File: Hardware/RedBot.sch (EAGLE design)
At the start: 40 parts, among them U1 ATMEGA328P, U2 TB6612FNG, U3 MIC5219 5V

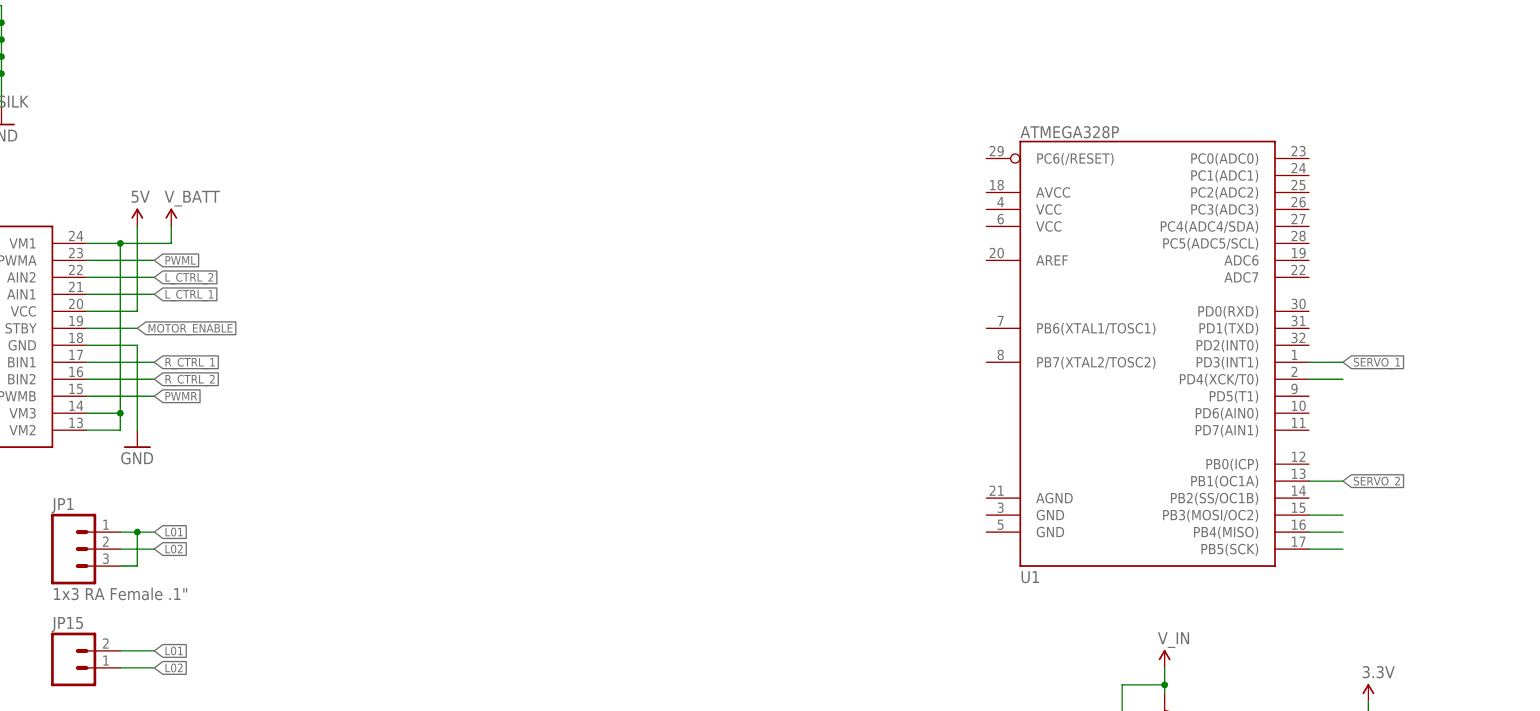
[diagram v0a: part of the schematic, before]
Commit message: Updated motor ic to use 3.3V
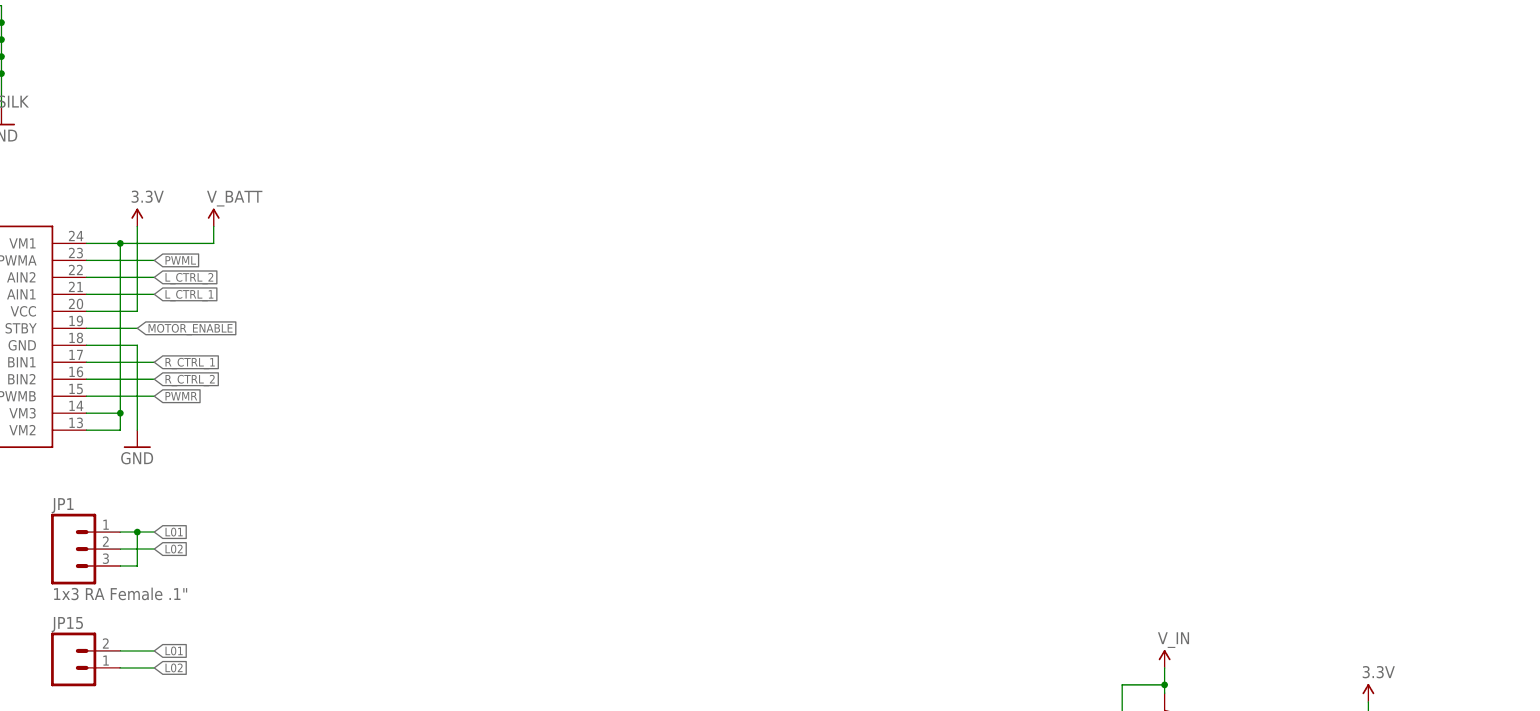
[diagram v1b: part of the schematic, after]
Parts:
- removed U1: ATMEGA328P, SparkFun-DigitalIC:ATMEGA328_SMT
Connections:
- removed net MISO: U1.PB4(MISO)
- removed net SCK: U1.PB5(SCK)
- removed net SERVO_4/MOSI: U1.PB3(MOSI/OC2)
- net 3.3V: now also U2.VCC
- net 5V: no longer U2.VCC
- net L_CTRL_2: no longer U1.PD4(XCK/T0)
- net SERVO_1: no longer U1.PD3(INT1)
- net SERVO_2: no longer U1.PB1(OC1A)
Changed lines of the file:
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@@
 <parts>
 <part name="FRAME1" library="SparkFun-Aesthetics" deviceset="FRAME-LETTER" device=""/>
-<part name="U1" library="SparkFun-DigitalIC" deviceset="ATMEGA328_SMT" device="" value="ATMEGA328P"/>
 <part name="C2" library="SparkFun-Capacitors" deviceset="0.1UF-25V(+80/-20%)(0603)" device="" value="0.1uF"/>
 <part name="C3" library="SparkFun-Capacitors" deviceset="0.1UF-25V(+80/-20%)(0603)" device="" value="0.1uF"/>
@@
 <part name="U$5" library="SparkFun-Aesthetics" deviceset="5V" device="" value="V_IN"/>
 <part name="U$7" library="SparkFun-Aesthetics" deviceset="V_BATT" device=""/>
-<part name="U$8" library="SparkFun-Aesthetics" deviceset="5V" device=""/>
+<part name="3.3V" library="SparkFun-Aesthetics" deviceset="5V" device="" value="3.3V"/>
 <part name="GND6" library="SparkFun-Aesthetics" deviceset="GND" device=""/>
 <part name="GND7" library="SparkFun-Aesthetics" deviceset="GND" device=""/>
@@
 <instances>
 <instance part="FRAME1" gate="G$2" x="304.8" y="0"/>
-<instance part="U1" gate="G$1" x="236.22" y="129.54"/>
 <instance part="C2" gate="G$1" x="300.99" y="63.5"/>
 <instance part="C3" gate="G$1" x="311.15" y="63.5"/>
@@
 <instance part="GND4" gate="1" x="240.03" y="10.16"/>
 <instance part="U$5" gate="G$1" x="240.03" y="78.74"/>
-<instance part="U$7" gate="G$1" x="91.44" y="144.78"/>
-<instance part="U$8" gate="G$1" x="86.36" y="144.78"/>
+<instance part="U$7" gate="G$1" x="97.79" y="144.78"/>
+<instance part="3.3V" gate="G$1" x="86.36" y="144.78"/>
 <instance part="GND6" gate="1" x="86.36" y="111.76"/>
 <instance part="GND7" gate="1" x="40.64" y="111.76"/>
@@
 <net name="SERVO_1" class="0">
 <segment>
-<pinref part="U1" gate="G$1" pin="PD3(INT1)"/>
-<wire x1="261.62" y1="124.46" x2="266.7" y2="124.46" width="0.1524" layer="91"/>
-<label x="266.7" y="124.46" size="1.27" layer="95" xref="yes"/>
-</segment>
-<segment>
 <pinref part="JP8" gate="G$1" pin="1"/>
 <wire x1="353.06" y1="185.42" x2="342.9" y2="185.42" width="0.1524" layer="91"/>
@@
 <net name="SERVO_2" class="0">
 <segment>
-<pinref part="U1" gate="G$1" pin="PB1(OC1A)"/>
-<wire x1="261.62" y1="106.68" x2="266.7" y2="106.68" width="0.1524" layer="91"/>
-<label x="266.7" y="106.68" size="1.27" layer="95" xref="yes"/>
-</segment>
-<segment>
 <pinref part="JP8" gate="G$1" pin="2"/>
 <wire x1="368.3" y1="185.42" x2="378.46" y2="185.42" width="0.1524" layer="91"/>
@@
 <wire x1="391.16" y1="231.14" x2="393.7" y2="231.14" width="0.1524" layer="91"/>
 <label x="393.7" y="231.14" size="1.27" layer="95" xref="yes"/>
-</segment>
-</net>
-<net name="SERVO_4/MOSI" class="0">
-<segment>
-<pinref part="U1" gate="G$1" pin="PB3(MOSI/OC2)"/>
-<wire x1="261.62" y1="101.6" x2="266.7" y2="101.6" width="0.1524" layer="91"/>
-</segment>
-</net>
-<net name="MISO" class="0">
-<segment>
-<pinref part="U1" gate="G$1" pin="PB4(MISO)"/>
-<wire x1="261.62" y1="99.06" x2="266.7" y2="99.06" width="0.1524" layer="91"/>
-</segment>
-</net>
-<net name="SCK" class="0">
-<segment>
-<pinref part="U1" gate="G$1" pin="PB5(SCK)"/>
-<wire x1="261.62" y1="96.52" x2="266.7" y2="96.52" width="0.1524" layer="91"/>
 </segment>
 </net>
@@
 </segment>
 <segment>
-<pinref part="U2" gate="G$1" pin="VCC"/>
-<wire x1="78.74" y1="132.08" x2="86.36" y2="132.08" width="0.1524" layer="91"/>
-<pinref part="U$8" gate="G$1" pin="5V"/>
-<wire x1="86.36" y1="132.08" x2="86.36" y2="144.78" width="0.1524" layer="91"/>
-</segment>
-<segment>
 <pinref part="R8" gate="G$1" pin="2"/>
 <wire x1="20.32" y1="231.14" x2="15.24" y2="231.14" width="0.1524" layer="91"/>
@@
 </segment>
 <segment>
-<pinref part="U1" gate="G$1" pin="PD4(XCK/T0)"/>
-<wire x1="261.62" y1="121.92" x2="266.7" y2="121.92" width="0.1524" layer="91"/>
-</segment>
-<segment>
 <pinref part="LAUNCHPAD" gate="G$1" pin="GPIO_I_D8"/>
 <wire x1="391.16" y1="220.98" x2="393.7" y2="220.98" width="0.1524" layer="91"/>
@@
 <pinref part="U2" gate="G$1" pin="VM2"/>
 <wire x1="78.74" y1="114.3" x2="83.82" y2="114.3" width="0.1524" layer="91"/>
-<wire x1="91.44" y1="144.78" x2="91.44" y2="142.24" width="0.1524" layer="91"/>
-<wire x1="91.44" y1="142.24" x2="83.82" y2="142.24" width="0.1524" layer="91"/>
+<wire x1="97.79" y1="144.78" x2="97.79" y2="142.24" width="0.1524" layer="91"/>
+<wire x1="97.79" y1="142.24" x2="83.82" y2="142.24" width="0.1524" layer="91"/>
 <pinref part="U2" gate="G$1" pin="VM3"/>
 <wire x1="83.82" y1="142.24" x2="83.82" y2="116.84" width="0.1524" layer="91"/>
@@
 <pinref part="P+1" gate="G$1" pin="3.3V"/>
 </segment>
-</net>
+<segment>
+<pinref part="U2" gate="G$1" pin="VCC"/>
+<wire x1="78.74" y1="132.08" x2="86.36" y2="132.08" width="0.1524" layer="91"/>
+<pinref part="3.3V" gate="G$1" pin="5V"/>
+<wire x1="86.36" y1="132.08" x2="86.36" y2="144.78" width="0.1524" layer="91"/>
+</segment>
+</net>
